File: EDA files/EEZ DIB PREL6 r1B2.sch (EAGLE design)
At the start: 65 parts, among them IC1 STM32F030C6T6, IC2 74HC1G126GW,125, IC3 M24C32-WMN6P, IC4 LP2985-33DBVR, K1 RT424005, K2 RT424005, K3 RT424005, K4 RT424005, K5 RT424005, K6 RT424005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

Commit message: #1 fixed
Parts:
- C2, C8, C9: device rcl:C-EUC1206 -> rcl:C-EUC0805
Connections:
- net +3V3: now also IC1.VDDA; no longer IC1.VSSA
- net GND: now also IC1.VSSA; no longer IC1.VDDA
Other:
- moved on the sheet: C5, C6
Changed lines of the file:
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@@
 <part name="SUPPLY66" library="supply2" deviceset="GND" device=""/>
 <part name="SUPPLY67" library="supply2" deviceset="GND" device=""/>
-<part name="C8" library="rcl" deviceset="C-EU" device="C1206" value="2u2"/>
+<part name="C8" library="rcl" deviceset="C-EU" device="C0805" value="2u2"/>
 <part name="P+1" library="supply1" deviceset="+5V" device=""/>
 <part name="P+2" library="supply1" deviceset="+5V" device=""/>
@@
 <part name="P+5" library="supply1" deviceset="+5V" device=""/>
 <part name="IC1" library="EEZ_DIB" deviceset="STM32F030" device="C6T6"/>
-<part name="SUPPLY48" library="supply2" deviceset="GND" device=""/>
 <part name="SUPPLY49" library="supply2" deviceset="GND" device=""/>
 <part name="C1" library="rcl" deviceset="C-EU" device="C0603" value="100n"/>
-<part name="C2" library="rcl" deviceset="C-EU" device="C1206" value="4u7"/>
+<part name="C2" library="rcl" deviceset="C-EU" device="C0805" value="4u7"/>
 <part name="SUPPLY61" library="supply2" deviceset="GND" device=""/>
 <part name="+3V4" library="supply1" deviceset="+3V3" device=""/>
@@
 <part name="C3" library="EEZ_Lib1" deviceset="ECAP" device="PANASONIC_H" value="EEEFK1V470P"/>
 <part name="SUPPLY45" library="supply2" deviceset="GND" device=""/>
-<part name="C9" library="rcl" deviceset="C-EU" device="C1206" value="4u7"/>
+<part name="C9" library="rcl" deviceset="C-EU" device="C0805" value="4u7"/>
 <part name="RN2" library="EEZ_Lib1" deviceset="R_ARRAY4" device="" value="DR1206-10K-4/8"/>
 <part name="+3V5" library="supply1" deviceset="+3V3" device=""/>
@@
 <part name="R7" library="rcl" deviceset="R-EU_" device="R0805" value="100K"/>
 <part name="X1" library="con-samtec" deviceset="SSW-106-02-S-S" device=""/>
+<part name="SUPPLY6" library="supply2" deviceset="GND" device=""/>
 </parts>
 <sheets>
@@
 <attribute name="VALUE" x="205.74" y="98.6536" size="2.0828" layer="96" ratio="6" rot="SR0"/>
 </instance>
-<instance part="SUPPLY48" gate="GND" x="172.72" y="81.28" smashed="yes">
-<attribute name="VALUE" x="170.815" y="81.915" size="1.778" layer="96" rot="R180"/>
-</instance>
-<instance part="SUPPLY49" gate="GND" x="223.52" y="63.5" smashed="yes">
-<attribute name="VALUE" x="225.425" y="64.135" size="1.778" layer="96" rot="MR180"/>
+<instance part="SUPPLY49" gate="GND" x="223.52" y="68.58" smashed="yes">
+<attribute name="VALUE" x="225.425" y="69.215" size="1.778" layer="96" rot="MR180"/>
 </instance>
 <instance part="C1" gate="G$1" x="195.58" y="144.78" smashed="yes" rot="MR90">
@@
 <attribute name="VALUE" x="248.285" y="140.335" size="1.778" layer="96" rot="MR180"/>
 </instance>
-<instance part="C6" gate="G$1" x="167.64" y="91.44" smashed="yes" rot="MR180">
-<attribute name="NAME" x="167.894" y="93.726" size="1.778" layer="95"/>
-<attribute name="VALUE" x="167.894" y="89.916" size="1.778" layer="96"/>
-</instance>
-<instance part="C5" gate="G$1" x="162.56" y="93.98" smashed="yes" rot="MR0">
-<attribute name="NAME" x="162.306" y="93.726" size="1.778" layer="95" rot="MR0"/>
-<attribute name="VALUE" x="162.306" y="89.916" size="1.778" layer="96" rot="MR0"/>
-</instance>
-<instance part="+3V2" gate="G$1" x="157.48" y="99.06" smashed="yes" rot="MR270">
-<attribute name="VALUE" x="156.845" y="100.33" size="1.778" layer="96" rot="R180"/>
+<instance part="C6" gate="G$1" x="172.72" y="93.98" smashed="yes">
+<attribute name="NAME" x="172.974" y="91.694" size="1.778" layer="95" rot="MR180"/>
+<attribute name="VALUE" x="172.974" y="95.504" size="1.778" layer="96" rot="MR180"/>
+</instance>
+<instance part="C5" gate="G$1" x="167.64" y="91.44" smashed="yes" rot="R180">
+<attribute name="NAME" x="167.386" y="91.694" size="1.778" layer="95" rot="R180"/>
+<attribute name="VALUE" x="167.386" y="95.504" size="1.778" layer="96" rot="R180"/>
+</instance>
+<instance part="+3V2" gate="G$1" x="162.56" y="86.36" smashed="yes" rot="R90">
+<attribute name="VALUE" x="161.925" y="85.09" size="1.778" layer="96" rot="MR0"/>
 </instance>
 <instance part="+3V3" gate="G$1" x="233.045" y="73.66" smashed="yes" rot="MR90">
@@
 <instance part="X1" gate="-4" x="177.8" y="165.1" smashed="yes" rot="MR0">
 <attribute name="NAME" x="180.848" y="165.862" size="1.524" layer="95" rot="MR180"/>
+</instance>
+<instance part="SUPPLY6" gate="GND" x="162.56" y="99.06" smashed="yes" rot="MR90">
+<attribute name="VALUE" x="160.655" y="98.425" size="1.778" layer="96" rot="MR0"/>
 </instance>
 </instances>
@@
 </segment>
 <segment>
-<pinref part="IC1" gate="G$1" pin="VDDA"/>
-<wire x1="182.88" y1="96.52" x2="172.72" y2="96.52" width="0.1524" layer="91"/>
-<wire x1="172.72" y1="96.52" x2="172.72" y2="86.36" width="0.1524" layer="91"/>
-<pinref part="SUPPLY48" gate="GND" pin="GND"/>
 <pinref part="C6" gate="G$1" pin="1"/>
-<wire x1="172.72" y1="86.36" x2="172.72" y2="83.82" width="0.1524" layer="91"/>
-<wire x1="172.72" y1="86.36" x2="167.64" y2="86.36" width="0.1524" layer="91"/>
-<wire x1="167.64" y1="86.36" x2="167.64" y2="88.9" width="0.1524" layer="91"/>
-<junction x="172.72" y="86.36"/>
+<wire x1="172.72" y1="99.06" x2="172.72" y2="96.52" width="0.1524" layer="91"/>
 <pinref part="C5" gate="G$1" pin="2"/>
-<wire x1="167.64" y1="86.36" x2="162.56" y2="86.36" width="0.1524" layer="91"/>
-<wire x1="162.56" y1="86.36" x2="162.56" y2="88.9" width="0.1524" layer="91"/>
-<junction x="167.64" y="86.36"/>
+<wire x1="172.72" y1="99.06" x2="167.64" y2="99.06" width="0.1524" layer="91"/>
+<wire x1="167.64" y1="99.06" x2="167.64" y2="96.52" width="0.1524" layer="91"/>
+<junction x="172.72" y="99.06"/>
+<pinref part="IC1" gate="G$1" pin="VSSA"/>
+<wire x1="172.72" y1="99.06" x2="182.88" y2="99.06" width="0.1524" layer="91"/>
+<pinref part="SUPPLY6" gate="GND" pin="GND"/>
+<wire x1="167.64" y1="99.06" x2="165.1" y2="99.06" width="0.1524" layer="91"/>
+<junction x="167.64" y="99.06"/>
 </segment>
 <segment>
 <pinref part="IC1" gate="G$1" pin="VSS_3"/>
-<wire x1="223.52" y1="76.2" x2="223.52" y2="66.04" width="0.1524" layer="91"/>
+<wire x1="223.52" y1="76.2" x2="223.52" y2="71.12" width="0.1524" layer="91"/>
 <pinref part="SUPPLY49" gate="GND" pin="GND"/>
 </segment>
@@
 </segment>
 <segment>
-<pinref part="IC1" gate="G$1" pin="VSSA"/>
-<wire x1="182.88" y1="99.06" x2="167.64" y2="99.06" width="0.1524" layer="91"/>
 <pinref part="C6" gate="G$1" pin="2"/>
-<wire x1="167.64" y1="99.06" x2="167.64" y2="96.52" width="0.1524" layer="91"/>
+<wire x1="172.72" y1="86.36" x2="172.72" y2="88.9" width="0.1524" layer="91"/>
 <pinref part="C5" gate="G$1" pin="1"/>
-<wire x1="167.64" y1="99.06" x2="162.56" y2="99.06" width="0.1524" layer="91"/>
-<wire x1="162.56" y1="99.06" x2="162.56" y2="96.52" width="0.1524" layer="91"/>
-<junction x="167.64" y="99.06"/>
-<wire x1="162.56" y1="99.06" x2="160.02" y2="99.06" width="0.1524" layer="91"/>
-<junction x="162.56" y="99.06"/>
+<wire x1="172.72" y1="86.36" x2="167.64" y2="86.36" width="0.1524" layer="91"/>
+<wire x1="167.64" y1="86.36" x2="167.64" y2="88.9" width="0.1524" layer="91"/>
+<wire x1="167.64" y1="86.36" x2="165.1" y2="86.36" width="0.1524" layer="91"/>
+<junction x="167.64" y="86.36"/>
 <pinref part="+3V2" gate="G$1" pin="+3V3"/>
-</segment>
-<segment>
+<pinref part="IC1" gate="G$1" pin="VDDA"/>
+<wire x1="182.88" y1="96.52" x2="177.8" y2="96.52" width="0.1524" layer="91"/>
+<wire x1="177.8" y1="96.52" x2="177.8" y2="86.36" width="0.1524" layer="91"/>
+<wire x1="177.8" y1="86.36" x2="172.72" y2="86.36" width="0.1524" layer="91"/>
+<junction x="172.72" y="86.36"/>
+</segment>
+<segment>

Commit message: #2
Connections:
- net BOOT0: now also X2-26.1
- net GND: no longer X2-26.1
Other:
- note added: "26 BOOT0"
- note removed: "26 Gnd"
- moved on the sheet: IC2A, RN2-1
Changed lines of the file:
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@@
 <setting verticaltext="up"/>
 </settings>
-<grid distance="0.1" unitdist="inch" unit="inch" style="lines" multiple="1" display="no" altdistance="0.01" altunitdist="inch" altunit="inch"/>
+<grid distance="0.025" unitdist="inch" unit="inch" style="lines" multiple="4" display="no" altdistance="0.01" altunitdist="inch" altunit="inch"/>
 <layers>
 <layer number="1" name="Top" color="4" fill="1" visible="no" active="no"/>
@@
 <circle x="118.11" y="156.21" radius="0.635" width="0.1524" layer="101"/>
 <circle x="118.11" y="153.67" radius="0.635" width="0.1524" layer="101"/>
-<text x="120.65" y="132.715" size="1.4224" layer="101">26 Gnd</text>
+<text x="120.65" y="132.715" size="1.4224" layer="101">26 BOOT0</text>
 <text x="113.03" y="156.845" size="1.4224" layer="101" rot="R180">Gnd 7</text>
 <text x="120.65" y="137.795" size="1.4224" layer="101">22 +12V</text>
@@
 </instance>
 <instance part="SUPPLY28" gate="GND" x="73.66" y="116.84" smashed="yes">
-<attribute name="VALUE" x="75.565" y="117.475" size="1.778" layer="96" rot="MR180"/>
+<attribute name="VALUE" x="71.755" y="117.475" size="1.778" layer="96" rot="R180"/>
 </instance>
 <instance part="C7" gate="G$1" x="58.42" y="50.8" smashed="yes" rot="R270">
@@
 <attribute name="VALUE" x="81.026" y="35.814" size="1.778" layer="96" rot="R180"/>
 </instance>
-<instance part="RN2" gate="-1" x="101.6" y="114.3" smashed="yes" rot="R90">
-<attribute name="VALUE" x="102.87" y="112.522" size="1.27" layer="96"/>
-<attribute name="NAME" x="102.87" y="114.427" size="1.27" layer="95"/>
-</instance>
-<instance part="+3V5" gate="G$1" x="101.6" y="124.46" smashed="yes">
-<attribute name="VALUE" x="102.87" y="123.825" size="1.778" layer="96"/>
+<instance part="RN2" gate="-1" x="96.52" y="114.3" smashed="yes" rot="R90">
+<attribute name="VALUE" x="97.79" y="112.522" size="1.27" layer="96"/>
+<attribute name="NAME" x="97.79" y="114.427" size="1.27" layer="95"/>
+</instance>
+<instance part="+3V5" gate="G$1" x="96.52" y="124.46" smashed="yes">
+<attribute name="VALUE" x="97.79" y="123.825" size="1.778" layer="96"/>
 </instance>
 <instance part="RN2" gate="-2" x="40.64" y="22.86" smashed="yes" rot="R180">
@@
 <attribute name="VALUE" x="125.73" y="123.825" size="1.778" layer="96"/>
 </instance>
-<instance part="IC2" gate="A" x="93.98" y="106.68" smashed="yes" rot="MR0">
-<attribute name="NAME" x="96.52" y="109.855" size="1.778" layer="95" rot="MR0"/>
-<attribute name="VALUE" x="94.615" y="101.6" size="1.27" layer="96"/>
+<instance part="IC2" gate="A" x="88.9" y="106.68" smashed="yes" rot="R180">
+<attribute name="NAME" x="89.535" y="109.855" size="1.778" layer="95"/>
+<attribute name="VALUE" x="83.185" y="103.505" size="1.27" layer="96" rot="MR180"/>
 </instance>
 <instance part="IC2" gate="B" x="124.46" y="111.76" smashed="yes" rot="MR0">
@@
 <wire x1="73.66" y1="139.7" x2="73.66" y2="134.62" width="0.1524" layer="91"/>
 <pinref part="X2" gate="-20" pin="1"/>
-<wire x1="73.66" y1="134.62" x2="73.66" y2="127" width="0.1524" layer="91"/>
-<wire x1="73.66" y1="127" x2="73.66" y2="119.38" width="0.1524" layer="91"/>
+<wire x1="73.66" y1="134.62" x2="73.66" y2="119.38" width="0.1524" layer="91"/>
 <wire x1="68.58" y1="134.62" x2="73.66" y2="134.62" width="0.1524" layer="91"/>
 <junction x="73.66" y="134.62"/>
-<pinref part="X2" gate="-26" pin="1"/>
-<wire x1="68.58" y1="127" x2="73.66" y2="127" width="0.1524" layer="91"/>
-<junction x="73.66" y="127"/>
 <pinref part="SUPPLY28" gate="GND" pin="GND"/>
 </segment>
@@
 <segment>
 <pinref part="RN2" gate="-1" pin="2"/>
-<wire x1="101.6" y1="119.38" x2="101.6" y2="121.92" width="0.1524" layer="91"/>
+<wire x1="96.52" y1="119.38" x2="96.52" y2="121.92" width="0.1524" layer="91"/>
 <pinref part="+3V5" gate="G$1" pin="+3V3"/>
 </segment>
@@
 </segment>
 <segment>
-<wire x1="93.98" y1="96.52" x2="106.68" y2="96.52" width="0.1524" layer="91"/>
-<label x="106.68" y="97.155" size="1.27" layer="102" rot="MR0"/>
+<wire x1="88.9" y1="127" x2="68.58" y2="127" width="0.1524" layer="91"/>
+<label x="96.52" y="127.635" size="1.27" layer="102" rot="MR0"/>
 <pinref part="IC2" gate="A" pin="EN"/>
-<wire x1="93.98" y1="96.52" x2="93.98" y2="101.6" width="0.1524" layer="91"/>
+<wire x1="88.9" y1="127" x2="88.9" y2="111.76" width="0.1524" layer="91"/>
+<wire x1="88.9" y1="127" x2="96.52" y2="127" width="0.1524" layer="91"/>
+<junction x="88.9" y="127"/>
+<pinref part="X2" gate="-26" pin="1"/>
 </segment>
 </net>
@@
 </segment>
 <segment>
-<wire x1="99.06" y1="106.68" x2="101.6" y2="106.68" width="0.1524" layer="91"/>
-<wire x1="101.6" y1="106.68" x2="114.3" y2="106.68" width="0.1524" layer="91"/>
-<wire x1="101.6" y1="106.68" x2="101.6" y2="109.22" width="0.1524" layer="91"/>
-<junction x="101.6" y="106.68"/>
+<wire x1="93.98" y1="106.68" x2="96.52" y2="106.68" width="0.1524" layer="91"/>
+<wire x1="96.52" y1="106.68" x2="109.22" y2="106.68" width="0.1524" layer="91"/>
+<wire x1="96.52" y1="106.68" x2="96.52" y2="109.22" width="0.1524" layer="91"/>
+<junction x="96.52" y="106.68"/>
 <pinref part="RN2" gate="-1" pin="1"/>
-<label x="114.3" y="107.315" size="1.27" layer="102" rot="MR0"/>
+<label x="109.22" y="107.315" size="1.27" layer="102" rot="MR0"/>
 <pinref part="IC2" gate="A" pin="I"/>
 </segment>
@@
 <segment>
 <pinref part="X2" gate="-28" pin="1"/>
-<wire x1="68.58" y1="124.46" x2="81.28" y2="124.46" width="0.1524" layer="91"/>
-<wire x1="81.28" y1="124.46" x2="81.28" y2="106.68" width="0.1524" layer="91"/>
-<wire x1="81.28" y1="106.68" x2="86.36" y2="106.68" width="0.1524" layer="91"/>
+<wire x1="68.58" y1="124.46" x2="76.2" y2="124.46" width="0.1524" layer="91"/>
+<wire x1="76.2" y1="124.46" x2="76.2" y2="106.68" width="0.1524" layer="91"/>
+<wire x1="76.2" y1="106.68" x2="81.28" y2="106.68" width="0.1524" layer="91"/>
 <pinref part="IC2" gate="A" pin="O"/>
 </segment>

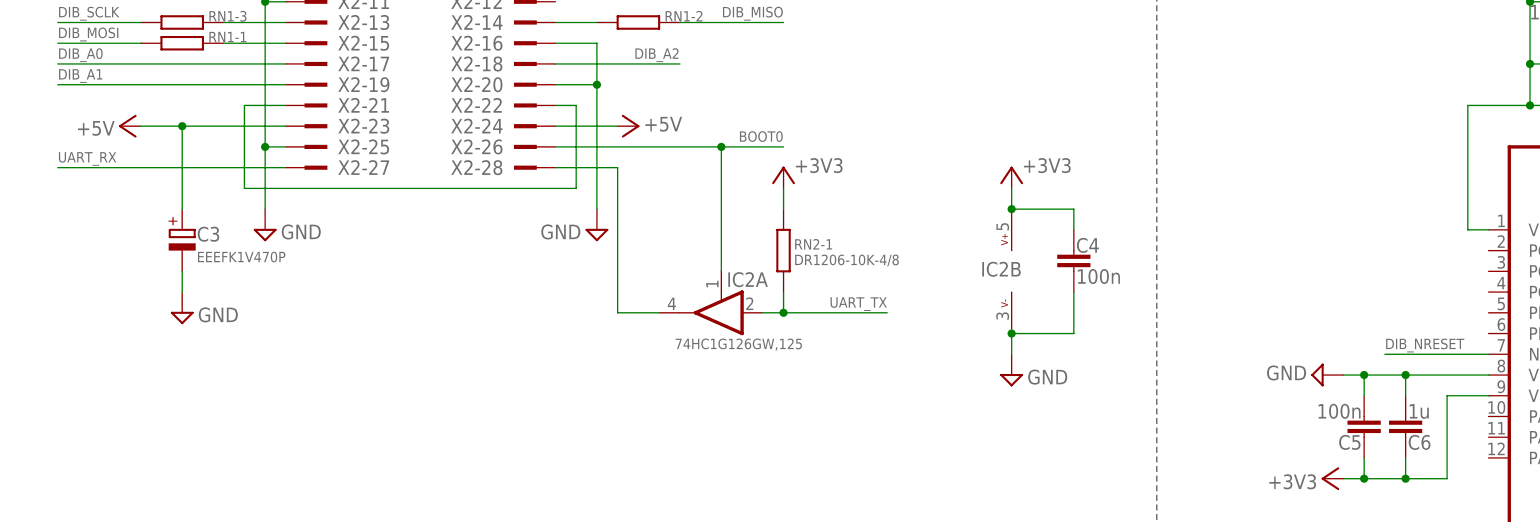
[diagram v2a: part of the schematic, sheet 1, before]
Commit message: swap UART TX and RX
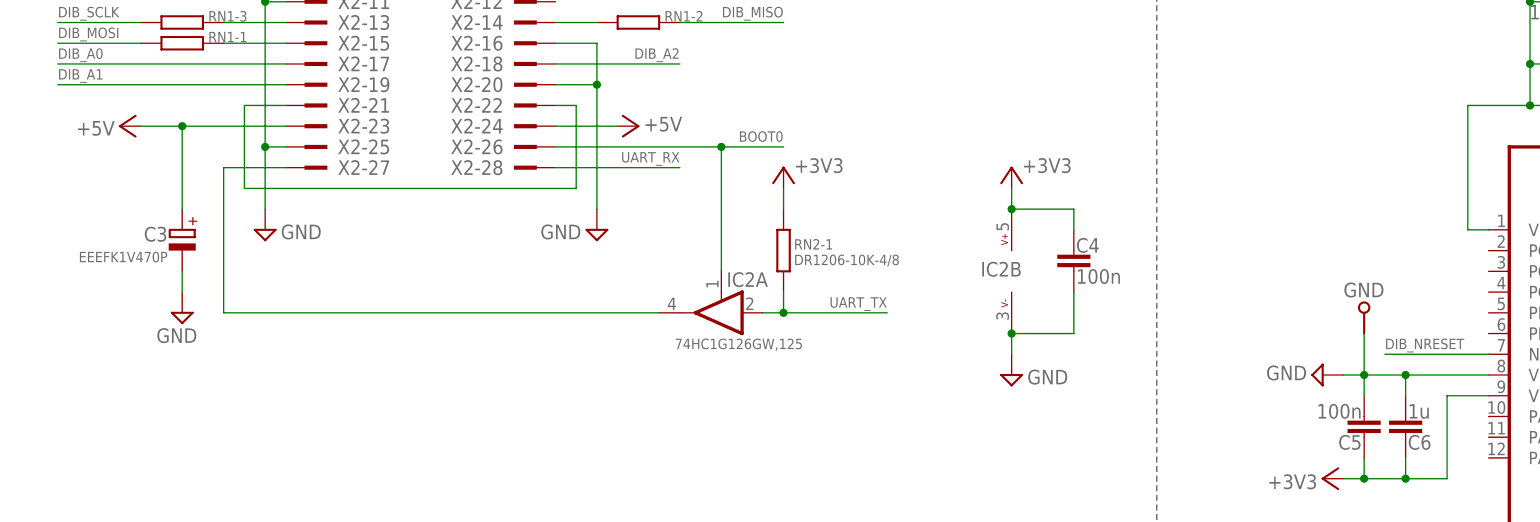
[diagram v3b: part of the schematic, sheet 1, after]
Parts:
- added GND: (no value), EEZ_Lib1:PCB_TEST_TABSHIELD
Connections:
- removed net N$72: IC2A.O, X2-28.1
- new net DIB_UART_RX: IC2A.O, X2-27.1
- net GND: now also GND.P$1
- net UART_RX: now also X2-28.1; no longer X2-27.1
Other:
- note added: "28 UART_TX"
- note added: "UART_RX 27"
- note removed: "28 UART_RX"
- note removed: "UART_TX 27"
- moved on the sheet: C3
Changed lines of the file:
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@@
 <setting verticaltext="up"/>
 </settings>
-<grid distance="0.025" unitdist="inch" unit="inch" style="lines" multiple="4" display="no" altdistance="0.01" altunitdist="inch" altunit="inch"/>
+<grid distance="0.1" unitdist="inch" unit="inch" style="lines" multiple="1" display="no" altdistance="0.01" altunitdist="inch" altunit="inch"/>
 <layers>
 <layer number="1" name="Top" color="4" fill="1" visible="no" active="no"/>
@@
 <part name="X1" library="con-samtec" deviceset="SSW-106-02-S-S" device=""/>
 <part name="SUPPLY6" library="supply2" deviceset="GND" device=""/>
+<part name="GND" library="EEZ_Lib1" deviceset="PCB_TEST_TAB" device="SHIELD"/>
 </parts>
 <sheets>
@@
 <circle x="115.57" y="130.81" radius="0.635" width="0.1524" layer="101"/>
 <circle x="118.11" y="130.81" radius="0.635" width="0.1524" layer="101"/>
-<text x="120.65" y="130.175" size="1.4224" layer="101">28 UART_RX</text>
-<text x="113.03" y="131.445" size="1.4224" layer="101" rot="R180">UART_TX 27</text>
+<text x="120.65" y="130.175" size="1.4224" layer="101">28 UART_TX</text>
+<text x="113.03" y="131.445" size="1.4224" layer="101" rot="R180">UART_RX 27</text>
 <text x="7.62" y="63.5" size="1.778" layer="97" rot="MR180">I2C Module ID EEPROM</text>
 <wire x1="142.24" y1="177.8" x2="142.24" y2="154.94" width="0.1524" layer="97" style="shortdash"/>
@@
 <attribute name="VALUE" x="233.68" y="74.93" size="1.778" layer="96" rot="MR180"/>
 </instance>
-<instance part="C3" gate="G$1" x="22.86" y="116.84" smashed="yes">
-<attribute name="NAME" x="24.638" y="115.4176" size="1.778" layer="95"/>
-<attribute name="VALUE" x="24.638" y="112.8776" size="1.27" layer="96"/>
+<instance part="C3" gate="G$1" x="22.86" y="116.84" smashed="yes" rot="MR0">
+<attribute name="NAME" x="21.082" y="115.4176" size="1.778" layer="95" rot="MR0"/>
+<attribute name="VALUE" x="21.082" y="112.8776" size="1.27" layer="96" rot="MR0"/>
 </instance>
 <instance part="SUPPLY45" gate="GND" x="22.86" y="106.68" smashed="yes">
-<attribute name="VALUE" x="24.765" y="107.315" size="1.778" layer="96" rot="MR180"/>
+<attribute name="VALUE" x="19.685" y="104.775" size="1.778" layer="96" rot="MR180"/>
 </instance>
 <instance part="C9" gate="G$1" x="81.28" y="35.56" smashed="yes" rot="R180">
@@
 <instance part="SUPPLY6" gate="GND" x="162.56" y="99.06" smashed="yes" rot="MR90">
 <attribute name="VALUE" x="160.655" y="98.425" size="1.778" layer="96" rot="MR0"/>
+</instance>
+<instance part="GND" gate="G$1" x="167.64" y="106.68" smashed="yes" rot="R90">
+<attribute name="NAME" x="165.1" y="108.585" size="1.778" layer="95"/>
+<attribute name="VALUE" x="170.18" y="106.68" size="1.778" layer="96" rot="R90"/>
 </instance>
 </instances>
@@
 <wire x1="167.64" y1="99.06" x2="165.1" y2="99.06" width="0.1524" layer="91"/>
 <junction x="167.64" y="99.06"/>
+<pinref part="GND" gate="G$1" pin="P$1"/>
+<wire x1="167.64" y1="99.06" x2="167.64" y2="104.14" width="0.1524" layer="91"/>
 </segment>
 <segment>
@@
 </segment>
 <segment>
-<pinref part="X2" gate="-27" pin="1"/>
-<wire x1="35.56" y1="124.46" x2="7.62" y2="124.46" width="0.1524" layer="91"/>
-<label x="7.62" y="125.095" size="1.27" layer="102"/>
+<pinref part="X2" gate="-28" pin="1"/>
+<wire x1="68.58" y1="124.46" x2="83.82" y2="124.46" width="0.1524" layer="91"/>
+<label x="83.82" y="125.095" size="1.27" layer="102" rot="MR0"/>
 </segment>
 </net>
@@
 </segment>
 </net>
-<net name="N$72" class="0">
-<segment>
-<pinref part="X2" gate="-28" pin="1"/>
-<wire x1="68.58" y1="124.46" x2="76.2" y2="124.46" width="0.1524" layer="91"/>
-<wire x1="76.2" y1="124.46" x2="76.2" y2="106.68" width="0.1524" layer="91"/>
-<wire x1="76.2" y1="106.68" x2="81.28" y2="106.68" width="0.1524" layer="91"/>
+<net name="DIB_UART_RX" class="0">
+<segment>
 <pinref part="IC2" gate="A" pin="O"/>
-</segment>
-</net>
+<wire x1="81.28" y1="106.68" x2="27.94" y2="106.68" width="0.1524" layer="91"/>
+<wire x1="27.94" y1="106.68" x2="27.94" y2="124.46" width="0.1524" layer="91"/>
+<pinref part="X2" gate="-27" pin="1"/>
+<wire x1="27.94" y1="124.46" x2="35.56" y2="124.46" width="0.1524" layer="91"/>
+</segment>
+</net>

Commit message: IRQ selection jumper
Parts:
- added DIB1.1: JP3-CUT-0805-ROTATED, EEZ_Lib1:JP3-CUT-0805-ROTATED
- C5: value 100n -> 1u; device rcl:C-EUC0603 -> rcl:C-EUC0805
- C6: value 1u -> 100n; device rcl:C-EUC0805 -> rcl:C-EUC0603
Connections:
- new net DIB_CSB: DIB1.1.NO, X2-12.1
- new net N$13: DIB1.1.COM, IC1.PA12
- net +3V3: now also C5.2, C6.1; no longer C5.1, C6.2
- net DIB_IRQ: now also DIB1.1.NC; no longer IC1.PA12
- net GND: now also C5.1, C6.2; no longer C5.2, C6.1
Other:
- note added: "DIB connector"
- note added: "JTAG/SWD (optional)"
- moved on the sheet: C1, C2, C5, C6, GND, IC1, R1
